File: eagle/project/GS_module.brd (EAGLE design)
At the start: 100 x 80 mm, 102 parts, among them IC1 LM358, Q2 MOSFET-PCHANNELFQP27P06, U1 V_REG_317SMD

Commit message: v1.0 of ETC board complete
initial work on GS board underway too
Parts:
- added U$20: (no value), custom:NURLOGO
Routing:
- net +5VCLEAN: track 316.0 -> 276.3 mm
- net GNDI: track 122.4 -> 96.0 mm, vias 17 -> 20
- net N$19: track 35.1 -> 33.6 mm
- net N$41: track 17.1 -> 18.0 mm
- added copper zone on layer 1, net GNDI
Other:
- board size 100 x 80 mm -> 101.3 x 81.3 mm
- board text added: "ETC module V1.0"
- board text added: "www.github.com/francisconroy"

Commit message: finish version 1.0 of GS board
yay!
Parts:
- removed ACTUALLYACS722: ACS722, SparkFun-AnalogIC:SO08
- removed C10, C14, C8: 0.1 uF, rcl:C1206
- removed C13, C26, C3: 0.1uF, resistor:C1206
- removed C15, C20, C21, C22, C23: 1nF, rcl:C1206
- removed C16, C17, C18, C24, C25, C4, C5, C7, C9: 0.1uF, rcl:C1206
- removed C19, C27: 1uF, rcl:C1206
- removed C28: 47uF, rcl:E5-8,5
- removed C29, C6: 10n, rcl:C1206
- removed CANCONN, MOTOR: (no value), con-wago-508:W237-132
- removed D1: 1N4004, diode:DO41-10
- removed D3: 7.5V, diode:ZDIO-7.5
- removed IC1: LM358, SparkFun-AnalogIC:DIP08
- removed LED1: FUSE HERE, LilyPad-Wearables:LED-1206
- removed R19: 10k, resistor:R1206
- removed R20: 4.7k, resistor:R1206
- removed R21: 1k, resistor:R1206
- removed R22: 3k, rcl:M1206
- removed R23: 2k, rcl:M1206
- removed R24, R36: 39, rcl:R1206
- removed R25: 240, rcl:R1206
- removed R26: 680, rcl:R1206
- removed R27: 33, rcl:R1206
- removed R28, R29, R31, R32, R33, R35: 20k, rcl:R1206
- removed R30, R34: 40k, rcl:R1206
- removed R37: 56k, rcl:R1206
- removed R38: 4k7, rcl:R1206
- removed R39: 9k1, rcl:R1206
- removed S2: DIRTY 5V, SparkFun-Electromechanical:SWITCH-SPDT_KIT
- removed TPSTOECU: (no value), con-wago-508:W237-133
- removed U$10, U$12, U$14, U$7: PNP_TRAN, custom:SOT23-3
- removed U$11, U$13, U$6, U$9: NPN_TRAN, custom:SOT23-3
- removed U$15, U$16: ACPLC87BT, custom:SO8STRETCH
- removed U$18, U$19: OPTOISOLATOR-2SOIC8, SparkFun-DiscreteSemi:SO08-2
- removed U$20: (no value), custom:NURLOGO
- removed U$8: DISP_CONN, custom:DISP_CONN
- removed U1: V_REG_317SMD, SparkFun-PowerIC:SOT223
- removed X1: (no value), con-wago-508:W237-12P
- added CLUTCH_SW: (no value), con-wago-508:W237-132
- added ENDSTOPS, MOTECSIGNAL, SHIFT: (no value), con-wago-508:W237-133
- added MODE_SEL: (no value), con-wago-508:W237-5P
- added SOLDVR1, SOLDVR2: (no value), SparkFun-Connectors:1X10_LOCK
- R1: value 270 -> 27; device resistor:R1206 -> rcl:R1206
- R10, R14, R18: value 270 -> 10k; device resistor:R1206 -> rcl:R1206
- R11, R15: device resistor:R1206 -> rcl:R1206
- R12, R16: value 4.7k -> 10k; device resistor:R1206 -> rcl:R1206
- R13, R17: value 1k -> 10k; device resistor:R1206 -> rcl:R1206
- R2: value 10k -> 27; device resistor:R1206 -> rcl:R1206
- R3: value 4.7k -> 15; device resistor:R1206 -> rcl:R1206
- R4: value 1k -> 15; device resistor:R1206 -> rcl:R1206
- U$2: value TB6559FG -> (none); device custom:HSOP16-P-300-1.00 -> custom:NURLOGO
- moved Q2 94.2 mm to (5.71, 27.3), turned to 180 degrees
- moved R5 92.8 mm to (8.89, 33.0), flipped to the bottom, turned to 90 degrees
- moved BAT_CONN 89.8 mm to (5.08, 36.2), turned to 270 degrees
- moved 10VZENER 88.4 mm to (7.62, 21.6), flipped to the bottom
- moved U$5 87.6 mm to (3.81, 12.1)
- moved R12 68.3 mm to (16.5, 68.6), flipped to the bottom, turned to 270 degrees
- moved U$4 67.6 mm to (41.9, 74.9), turned to 180 degrees
- moved R14 65.1 mm to (11.4, 59.7), flipped to the bottom, turned to 180 degrees
- moved R15 61.6 mm to (11.4, 54.6), flipped to the bottom, turned to 180 degrees
- moved R16 60.9 mm to (11.4, 49.5), flipped to the bottom
- moved U$2 59.9 mm to (55.2, 10.2), turned to 0 degrees
- moved R13 57.6 mm to (21.6, 68.6), flipped to the bottom, turned to 270 degrees
- moved U$3 56.0 mm to (41.9, 68.6)
- moved R17 54.9 mm to (11.4, 44.5), flipped to the bottom, turned to 180 degrees
- moved R2 43.6 mm to (45.7, 50.2), flipped to the bottom
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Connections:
- removed net +5V/1: C13.1, C25.2, R7.1, S2.3, U$15.1, U$17.6, U$17.8, U$18.6, U$18.8, U$7.2
- removed net +5VCLEAN: C17.2, C24.2, C3.1, C4.2, IC1.8, R11.1, R15.1, R19.1, R2.1, S1.3, U$10.2, U$12.2, U$14.2, U$15.8, U$16.8, U$19.8, U$4.2, U$5.6, U$8.4
- removed net 5VOUT: C10.2, U$2.VREF, U$2.VREG
- removed net ECU5V: C16.2, TPSTOECU.1, U$16.1, X1.1
- removed net ECUSENSGND: C16.1, C6.2, R23.1, TPSTOECU.2, U$16.3, U$16.4, X1.2
- removed net ECUTPS: R22.2, TPSTOECU.3, X1.3
- removed net N$11: R8.1, U$6.1
- removed net N$12: R19.2, U$13.3, U$14.1
- removed net N$14: R18.1, U$18.3
- removed net N$15: C26.1, D3.C, LED1.C, S2.2
- removed net N$16: R37.2, R38.1
- removed net N$17: C19.1, D1.A, LED1.A, R25.2, U1.2
- removed net N$18: R11.2, U$10.1, U$9.3
- removed net N$19: MOTOR.1, U$2.OUT2
- removed net N$20: ACTUALLYACS722.1, ACTUALLYACS722.2, U$2.OUT1
- removed net N$21: R10.1, U$17.3
- removed net N$22: R10.2, U$10.3
- removed net N$23: R12.1, U$9.1
- removed net N$25: R15.2, U$11.3, U$12.1
- removed net N$26: R14.1, U$18.1
- removed net N$27: R14.2, U$12.3
- removed net N$28: R16.1, U$11.1
- removed net N$29: R17.1, U$18.7, U$2.IN2
- removed net N$30: R18.2, U$14.3
- removed net N$31: R20.1, U$13.1
- removed net N$32: R8.2, U$2.ALERT
- removed net N$33: R21.1, U$18.5, U$2.SB
- removed net N$34: ACTUALLYACS722.3, ACTUALLYACS722.4, MOTOR.2
- removed net N$35: C6.1, R24.1, U$16.2
- removed net N$36: R22.1, R23.2, R24.2
- removed net N$37: R26.1, R27.2
- removed net N$38: R25.1, R26.2, U1.1
- removed net N$39: R36.2, R37.1, R39.2
- removed net N$40: C23.1, IC1.5, R33.1, R35.1
- removed net N$41: C22.2, IC1.6, R32.1, R34.2
- removed net N$42: R32.2, U$15.6
- removed net N$43: R13.1, U$17.5, U$2.IN1
- removed net N$44: R29.2, U$16.7
- removed net N$45: C21.1, IC1.3, R29.1, R31.1
- removed net N$46: C20.2, IC1.2, R28.1, R30.2
- removed net N$47: R28.2, U$16.6
- removed net N$48: C29.1, R36.1, U$15.2
- removed net N$52: R33.2, U$15.7
- new net +5V: S1.3, SOLDVR1.10, SOLDVR2.10, U$17.8, U$5.6
- new net +5V/4: MOTECSIGNAL.1, R7.1, U$4.2
- new net GND4: MOTECSIGNAL.3, U$17.2, U$3.2
- net +12V: no longer C18.1, C27.1, C28.+, D1.C, R38.2, U$2.VCC, U1.3
- net +3V3: now also R10.2, R11.2, R12.2, R13.2, R14.2, R15.2, R16.2, R17.2, R18.2; no longer ACTUALLYACS722.8, C14.1, C5.2, C7.2, C8.1, C9.1, U$8.5, X1.10, X1.4, X1.7
- net AGND: now also R1.1, R2.1; no longer ACTUALLYACS722.5, ACTUALLYACS722.6, C14.2, C17.1, C24.1, C7.1, C8.2, C9.2, U$15.5, U$16.5, X1.11, X1.5, X1.8
- net GND: now also CLUTCH_SW.1, ENDSTOPS.1, MODE_SEL.5, SHIFT.1, SOLDVR1.9, SOLDVR2.9; no longer C15.2, C21.2, C23.2, C3.2, C4.1, C5.1, IC1.4, R31.2, R35.2, U$11.2, U$13.2, U$17.2, U$17.4, U$18.2, U$18.4, U$3.2, U$8.3, U$9.2
- net GNDI: no longer C10.1, C13.2, C18.2, C19.2, C25.1, C26.2, C27.2, C28.-, C29.2, D3.A, R13.2, R17.2, R21.2, R27.1, R39.1, R4.2, S2.1, U$15.3, U$15.4, U$19.2, U$2.FIN, U$2.FIN2, U$2.P$20, U$2.P$4, U$2.P-GND, U$2.RSA, U$2.S-GND, U$2.S-GND2, U$2.S-GND3, U$6.2
- net N$1: now also R7.2; no longer R2.2
- net N$10: now also SOLDVR1.1, SOLDVR2.1; no longer R6.2, U$7.3
- net N$3: now also R3.2, SOLDVR1.2; no longer R1.1, U$17.1
- net N$4: now also R6.1, U$17.1; no longer R1.2, U$4.3
- net N$5: now also R4.2, SOLDVR2.2; no longer R3.1, U$3.1
- net N$6: now also R6.2, U$4.3; no longer R7.2, U$6.3, U$7.1
- net N$8: now also R8.1, U$3.1; no longer R4.1, U$17.7, U$2.PWM
- net N$9: now also MOTECSIGNAL.2, R8.2; no longer R6.1, U$19.1
- net P10: now also SOLDVR2.6
- net P13: now also R9.1, U$17.7
- net P14: now also R10.1, SHIFT.3; no longer X1.9
- net P15: now also R11.1, SHIFT.2; no longer X1.12
- net P16: now also R1.2, R3.1; no longer C20.1, IC1.1, R30.1
- net P17: now also ENDSTOPS.3, R12.1; no longer X1.6
- net P18: now also ENDSTOPS.2, R13.1; no longer U$8.2
- net P19: now also R2.2, R4.1; no longer U$8.1
- net P2: now also SOLDVR1.5
- net P20: now also MODE_SEL.4, R14.1
- net P21: now also MODE_SEL.3, R15.1; no longer C22.1, IC1.7, R34.1
- net P22: now also MODE_SEL.2, R16.1; no longer ACTUALLYACS722.7, C15.1
- net P23: now also MODE_SEL.1, R17.1
- net P3: now also SOLDVR1.8; no longer CANCONN.1
- net P4: now also SOLDVR1.7; no longer CANCONN.2
- net P5: now also SOLDVR1.6; no longer R9.1, U$19.7
- net P6: now also CLUTCH_SW.2, R18.1; no longer R3.2
- net P7: now also SOLDVR2.5; no longer R12.2
- net P8: now also SOLDVR2.8; no longer R16.2
- net P9: now also SOLDVR2.7; no longer R20.2
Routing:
- net +5VCLEAN: track 276.3 -> 0.00 mm, vias 10 -> 0
- net +12V: track 183.3 -> 18.1 mm
- net +5V: track 0.00 -> 132.9 mm
- net +5V/1: track 123.2 -> 0.00 mm, vias 4 -> 0
- net AGND: track 158.1 -> 62.0 mm, vias 10 -> 2
- net GNDI: track 96.0 -> 19.8 mm, vias 20 -> 0
- net N$43: track 56.4 -> 0.00 mm, vias 2 -> 0
- net P20: track 3.56 -> 50.4 mm, vias 0 -> 2
- net ECUSENSGND: track 45.4 -> 0.00 mm, vias 2 -> 0
- net ECU5V: track 39.1 -> 0.00 mm, vias 2 -> 0
- net N$19: track 33.6 -> 0.00 mm
- net N$3: track 35.7 -> 3.11 mm
- net N$10: track 4.87 -> 36.6 mm, vias 0 -> 1
- net N$33: track 31.6 -> 0.00 mm, vias 2 -> 0
- net P23: track 4.06 -> 35.0 mm, vias 0 -> 2
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- removed copper zone on layer 1, net GNDI
- removed copper zone on layer 16, net GNDI
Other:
- board size 101.3 x 81.3 mm -> 67 x 81.3 mm
- board text added: "GS Module V1.0"
- board text added: "REAL, REAL QUICK"
- board text added: "S.T.I.G."
- board text added: "Sequential Transmission Interface Gizmo"
- board text added: "github.com/francisconroy"
- board text removed: "ETC module V1.0"
- board text removed: "www.github.com/francisconroy"

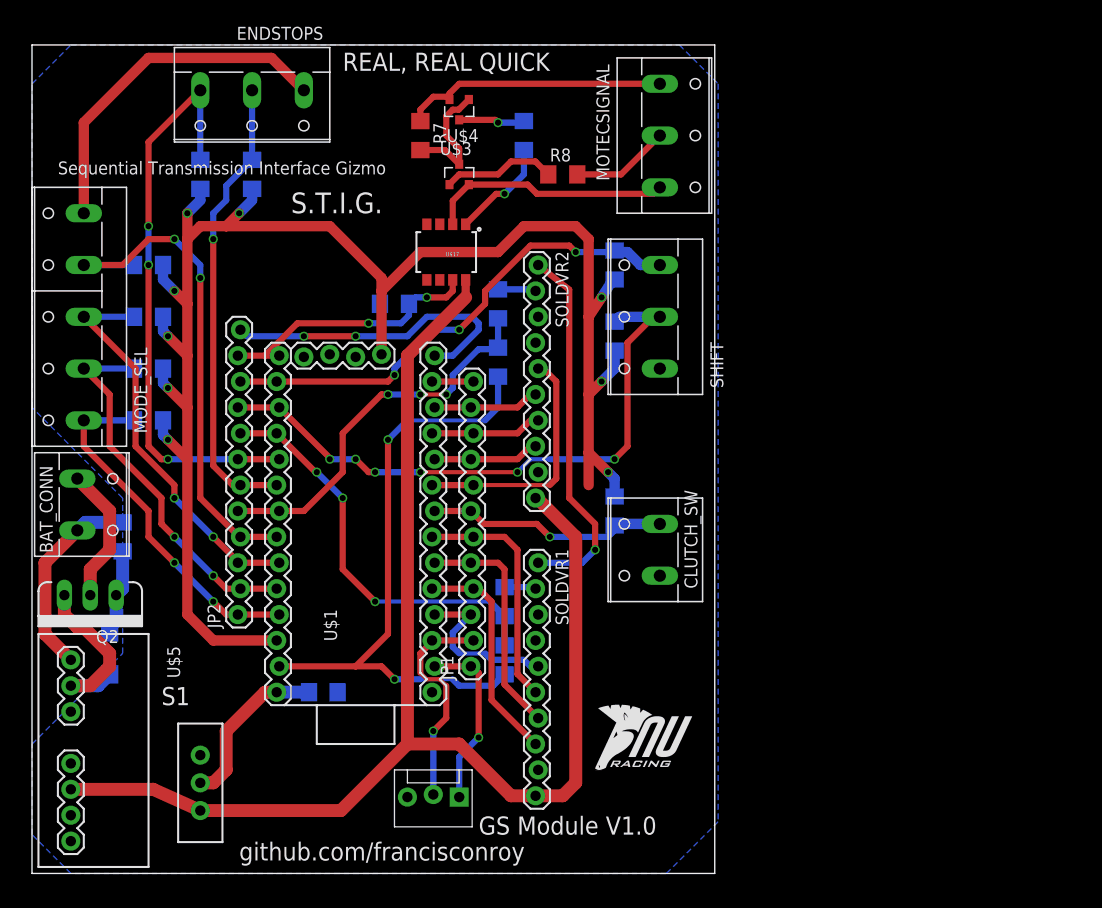
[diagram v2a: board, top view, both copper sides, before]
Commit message: Versions of the board which went to the fab house
Updating BOMS for component ordering
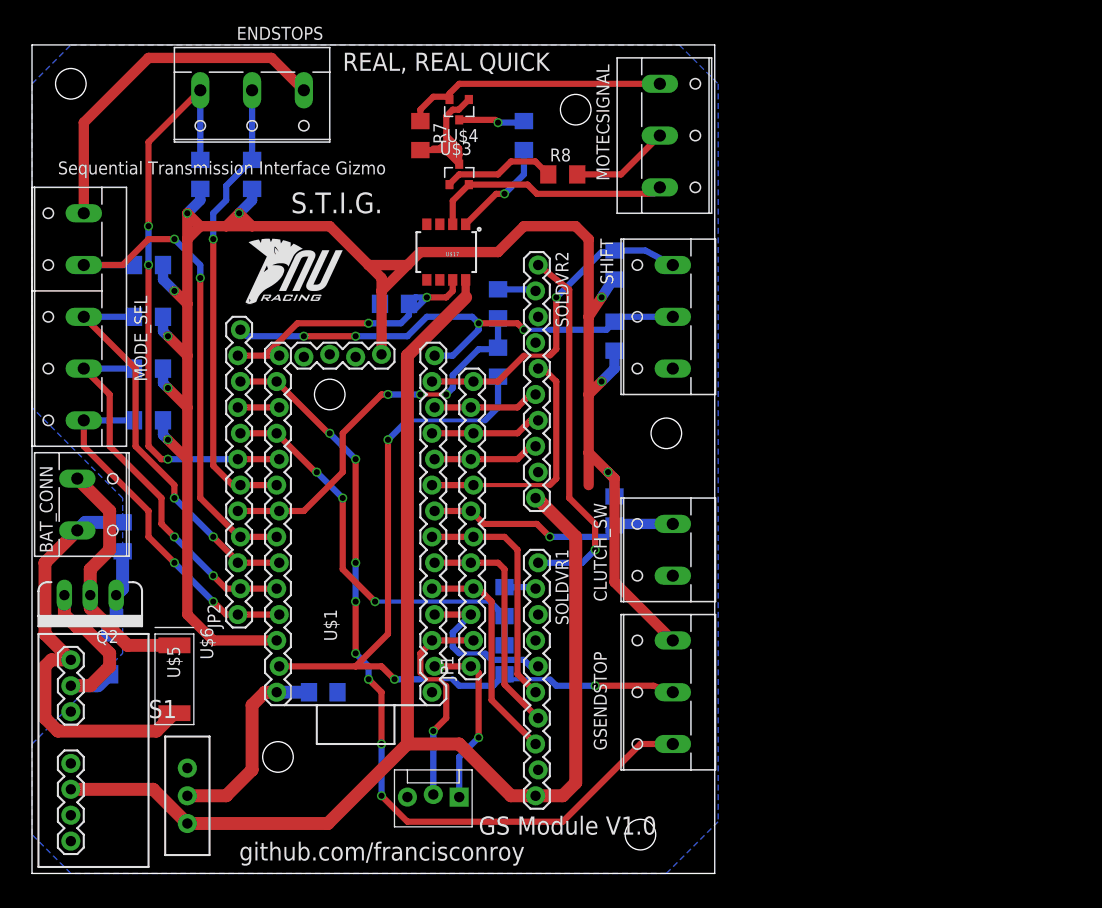
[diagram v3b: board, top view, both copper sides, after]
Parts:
- added GSENDSTOP: (no value), con-wago-508:W237-133
- added U$6: LNBTVS, custom:JEDECDO-214AB
- moved U$2 57.1 mm to (21.0, 55.9)
- moved S1 1.80 mm to (15.2, 7.62)
- moved CLUTCH_SW 1.27 mm to (62.2, 31.8)
- moved SHIFT 1.27 mm to (62.2, 54.6)
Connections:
- net +3V3: now also GSENDSTOP.3
- net AGND: now also GSENDSTOP.2
- net GNDI: now also U$6.A
- net N$13: now also U$6.K
- net P11: now also R10.1, SHIFT.3
- net P12: now also R11.1, SHIFT.2
- net P14: now also GSENDSTOP.1; no longer R10.1, SHIFT.3
- net P15: no longer R11.1, SHIFT.2
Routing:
- net P15: track 61.0 -> 4.06 mm, vias 6 -> 0
- net P14: track 48.7 -> 81.3 mm, vias 3 -> 8
- net P11: track 4.06 -> 32.3 mm, vias 0 -> 1
- net +3V3: track 168.0 -> 194.5 mm
- net GNDI: track 19.8 -> 41.7 mm
- net P12: track 30.7 -> 50.5 mm, vias 2 -> 4
- net AGND: track 62.0 -> 79.1 mm, vias 2 -> 3
- net N$13: track 13.5 -> 24.6 mm
- net N$1: track 12.5 -> 18.0 mm
- net N$2: track 16.8 -> 20.0 mm
- net P13: track 27.0 -> 28.8 mm
- net +12V: track 18.1 -> 19.7 mm
- net +5V: track 132.9 -> 134.3 mm
- net P6: track 24.0 -> 25.2 mm
